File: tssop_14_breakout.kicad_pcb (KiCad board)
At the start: 2 copper layers, 10.2 x 17.8 mm, 3 parts, among them J1 CONN_01X07, J2 CONN_01X07, U1 TSSOP-14

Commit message: Fixup silkscreen layers.
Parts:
- U1: value TSSOP-14 -> TSSOP
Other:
- board text added: "1"
- board text added: "14"
- board text added: "7"
- board text added: "8"
- board text added: "rpwoodbu v1"
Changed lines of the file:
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@@
     (area 148.514999 100.254999 158.825001 118.185001)
     (thickness 1.6)
-    (drawings 4)
+    (drawings 9)
     (tracks 75)
     (zones 0)
@@
     (descr "Through hole straight pin header, 1x07, 2.54mm pitch, single row")
     (tags "Through hole pin header THT 1x07 2.54mm single row")
-    (fp_text reference J1 (at 0 2.33 180) (layer B.SilkS)
+    (fp_text reference J1 (at 0 2.33 180) (layer B.SilkS) hide
       (effects (font (size 1 1) (thickness 0.15)) (justify mirror))
     )
@@
     (descr "Through hole straight pin header, 1x07, 2.54mm pitch, single row")
     (tags "Through hole pin header THT 1x07 2.54mm single row")
-    (fp_text reference J2 (at 0 2.33 180) (layer B.SilkS)
+    (fp_text reference J2 (at 0 2.33 180) (layer B.SilkS) hide
       (effects (font (size 1 1) (thickness 0.15)) (justify mirror))
     )
@@
     (tags "SSOP 0.65")
     (attr smd)
-    (fp_text reference U1 (at 0 -3.55 90) (layer F.SilkS)
+    (fp_text reference U1 (at 0 -3.55 90) (layer F.SilkS) hide
       (effects (font (size 1 1) (thickness 0.15)))
     )
-    (fp_text value TSSOP-14 (at 0 3.55 90) (layer F.Fab)
-      (effects (font (size 1 1) (thickness 0.15)))
+    (fp_text value TSSOP (at 4.49 0 180) (layer F.SilkS)
+      (effects (font (size 0.75 0.75) (thickness 0.1875)))
     )
     (fp_line (start -1.2 -2.5) (end 2.2 -2.5) (layer F.Fab) (width 0.15))
@@
     )
   )
+  (gr_text 8 (at 156.21 116.84) (layer F.SilkS)
+    (effects (font (size 1.5 1.5) (thickness 0.3)) (justify right))
+  )
+  (gr_text 7 (at 151.13 116.84) (layer F.SilkS)
+    (effects (font (size 1.5 1.5) (thickness 0.3)) (justify left))
+  )
+  (gr_text 14 (at 156.21 101.6) (layer F.SilkS)
+    (effects (font (size 1.5 1.5) (thickness 0.3)) (justify right))
+  )
+  (gr_text 1 (at 151.13 101.6) (layer F.SilkS)
+    (effects (font (size 1.5 1.5) (thickness 0.3)) (justify left))
+  )
+  (gr_text "rpwoodbu\nv1" (at 153.67 116.84) (layer B.SilkS)
+    (effects (font (size 0.5 0.5) (thickness 0.125)) (justify mirror))
+  )
   (gr_line (start 148.59 118.11) (end 148.59 100.33) (layer Edge.Cuts) (width 0.15))

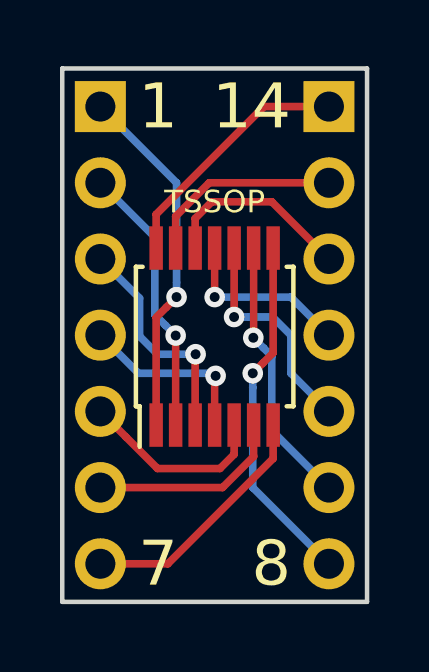
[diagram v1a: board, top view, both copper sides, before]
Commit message: Update netlist and layout with new tssop footprint
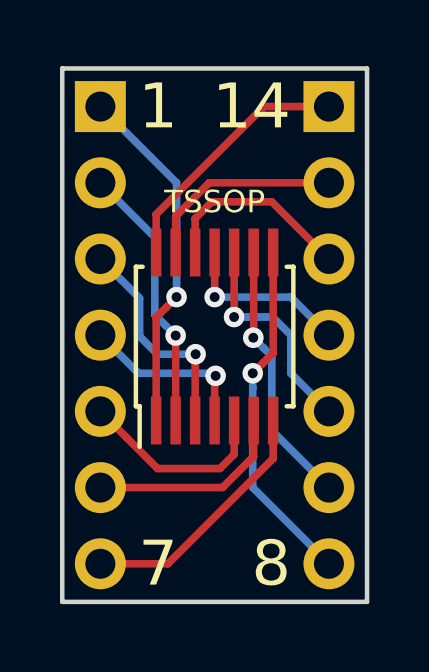
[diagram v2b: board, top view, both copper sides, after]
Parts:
- U1: footprint Housings_SSOP:TSSOP-14_4.4x5mm_Pitch0.65mm -> TSSOP:TSSOP-14_4.4x5mm_Pitch0.65mm
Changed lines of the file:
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@@
-(kicad_pcb (version 4) (host pcbnew 4.0.6-e0-6349~53~ubuntu16.04.1)
+(kicad_pcb (version 4) (host pcbnew 4.0.6-e0-6349~53~ubuntu14.04.1)
   (general
     (links 14)
@@
     )
   )
-  (module Housings_SSOP:TSSOP-14_4.4x5mm_Pitch0.65mm (layer F.Cu)
+  (module TSSOP:TSSOP-14_4.4x5mm_Pitch0.65mm (layer F.Cu)
     (at 153.67 109.265 90)
-    (descr "14-Lead Plastic Thin Shrink Small Outline (ST)-4.4 mm Body [TSSOP] (see Microchip Packaging Specification 00000049BS.pdf)")
+    (descr "14-Lead Plastic Thin Shrink Small Outline (ST)-4.4 mm Body [TSSOP]")
     (tags "SSOP 0.65")
     (attr smd)
@@
       (effects (font (size 0.8 0.8) (thickness 0.15)))
     )
-    (pad 1 smd rect (at -2.95 -1.95 90) (size 1.45 0.45) (layers F.Cu F.Paste F.Mask)
+    (pad 1 smd rect (at -2.8 -1.95 90) (size 1.6 0.35) (layers F.Cu F.Paste F.Mask)
       (net 1 "Net-(J1-Pad1)"))
-    (pad 2 smd rect (at -2.95 -1.3 90) (size 1.45 0.45) (layers F.Cu F.Paste F.Mask)
+    (pad 2 smd rect (at -2.8 -1.3 90) (size 1.6 0.35) (layers F.Cu F.Paste F.Mask)
       (net 2 "Net-(J1-Pad2)"))
-    (pad 3 smd rect (at -2.95 -0.65 90) (size 1.45 0.45) (layers F.Cu F.Paste F.Mask)
+    (pad 3 smd rect (at -2.8 -0.65 90) (size 1.6 0.35) (layers F.Cu F.Paste F.Mask)
       (net 3 "Net-(J1-Pad3)"))
-    (pad 4 smd rect (at -2.95 0 90) (size 1.45 0.45) (layers F.Cu F.Paste F.Mask)
+    (pad 4 smd rect (at -2.8 0 90) (size 1.6 0.35) (layers F.Cu F.Paste F.Mask)
       (net 4 "Net-(J1-Pad4)"))
-    (pad 5 smd rect (at -2.95 0.65 90) (size 1.45 0.45) (layers F.Cu F.Paste F.Mask)
+    (pad 5 smd rect (at -2.8 0.65 90) (size 1.6 0.35) (layers F.Cu F.Paste F.Mask)
       (net 5 "Net-(J1-Pad5)"))
-    (pad 6 smd rect (at -2.95 1.3 90) (size 1.45 0.45) (layers F.Cu F.Paste F.Mask)
+    (pad 6 smd rect (at -2.8 1.3 90) (size 1.6 0.35) (layers F.Cu F.Paste F.Mask)
       (net 6 "Net-(J1-Pad6)"))
-    (pad 7 smd rect (at -2.95 1.95 90) (size 1.45 0.45) (layers F.Cu F.Paste F.Mask)
+    (pad 7 smd rect (at -2.8 1.95 90) (size 1.6 0.35) (layers F.Cu F.Paste F.Mask)
       (net 7 "Net-(J1-Pad7)"))
-    (pad 8 smd rect (at 2.95 1.95 90) (size 1.45 0.45) (layers F.Cu F.Paste F.Mask)
+    (pad 8 smd rect (at 2.8 1.95 90) (size 1.6 0.35) (layers F.Cu F.Paste F.Mask)
       (net 14 "Net-(J2-Pad7)"))
-    (pad 9 smd rect (at 2.95 1.3 90) (size 1.45 0.45) (layers F.Cu F.Paste F.Mask)
+    (pad 9 smd rect (at 2.8 1.3 90) (size 1.6 0.35) (layers F.Cu F.Paste F.Mask)
       (net 13 "Net-(J2-Pad6)"))
-    (pad 10 smd rect (at 2.95 0.65 90) (size 1.45 0.45) (layers F.Cu F.Paste F.Mask)
+    (pad 10 smd rect (at 2.8 0.65 90) (size 1.6 0.35) (layers F.Cu F.Paste F.Mask)
       (net 12 "Net-(J2-Pad5)"))
-    (pad 11 smd rect (at 2.95 0 90) (size 1.45 0.45) (layers F.Cu F.Paste F.Mask)
+    (pad 11 smd rect (at 2.8 0 90) (size 1.6 0.35) (layers F.Cu F.Paste F.Mask)
       (net 11 "Net-(J2-Pad4)"))
-    (pad 12 smd rect (at 2.95 -0.65 90) (size 1.45 0.45) (layers F.Cu F.Paste F.Mask)
+    (pad 12 smd rect (at 2.8 -0.65 90) (size 1.6 0.35) (layers F.Cu F.Paste F.Mask)
       (net 10 "Net-(J2-Pad3)"))
-    (pad 13 smd rect (at 2.95 -1.3 90) (size 1.45 0.45) (layers F.Cu F.Paste F.Mask)
+    (pad 13 smd rect (at 2.8 -1.3 90) (size 1.6 0.35) (layers F.Cu F.Paste F.Mask)
       (net 9 "Net-(J2-Pad2)"))
-    (pad 14 smd rect (at 2.95 -1.95 90) (size 1.45 0.45) (layers F.Cu F.Paste F.Mask)
+    (pad 14 smd rect (at 2.8 -1.95 90) (size 1.6 0.35) (layers F.Cu F.Paste F.Mask)
       (net 8 "Net-(J2-Pad1)"))
     (model ${KISYS3DMOD}/Housings_SSOP.3dshapes/TSSOP-14_4.4x5mm_Pitch0.65mm.wrl

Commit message: Make back silkscreen more interesting.
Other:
- board text added: "github.com/ rpwoodbu/ tssop_14_breakout"
- board text added: "rpwoodbu jbebel v1"
- board text removed: "rpwoodbu v1"
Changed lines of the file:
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@@
-(kicad_pcb (version 4) (host pcbnew 4.0.6-e0-6349~53~ubuntu14.04.1)
+(kicad_pcb (version 4) (host pcbnew 4.0.6-e0-6349~53~ubuntu16.04.1)
   (general
     (links 14)
@@
     (area 148.514999 100.254999 158.825001 118.185001)
     (thickness 1.6)
-    (drawings 9)
+    (drawings 10)
     (tracks 75)
     (zones 0)
@@
     )
   )
+  (gr_text "github.com/\nrpwoodbu/\ntssop_14_breakout" (at 153.67 117.856 270) (layer B.SilkS)
+    (effects (font (size 0.5 0.5) (thickness 0.125)) (justify left mirror))
+  )
   (gr_text 8 (at 156.21 116.84) (layer F.SilkS)
     (effects (font (size 1.5 1.5) (thickness 0.3)) (justify right))
@@
     (effects (font (size 1.5 1.5) (thickness 0.3)) (justify left))
   )
-  (gr_text "rpwoodbu\nv1" (at 153.67 116.84) (layer B.SilkS)
-    (effects (font (size 0.5 0.5) (thickness 0.125)) (justify mirror))
+  (gr_text "rpwoodbu\njbebel\nv1" (at 153.67 100.584 270) (layer B.SilkS)
+    (effects (font (size 0.5 0.5) (thickness 0.125)) (justify right mirror))
   )
   (gr_line (start 148.59 118.11) (end 148.59 100.33) (layer Edge.Cuts) (width 0.15))
